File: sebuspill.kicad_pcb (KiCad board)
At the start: 2 copper layers, 67 x 26 mm, 30 parts, among them J1 Conn_01x04_Male, J2 USB_B_Micro, J3 Pinout 1, J4 Pinout 2, SW1 SW_SPDT, U1 AMS1117-3.3, U2 STM32F103C8T6, Y1 16MHz

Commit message: finished i think
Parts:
-  : renamed from U1
-  : renamed from SW1
- moved C11 6.83 mm to (150.0, 108.0), turned to -90 degrees
- moved R2 0.69 mm to (152.4, 97.5)
- renumbered D1 to LED
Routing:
- net PC13: track 0.00 -> 67.0 mm, vias 0 -> 6
- net VBUS: track 19.3 -> 80.7 mm, vias 0 -> 1
- net PB12: track 2.81 -> 54.6 mm, vias 1 -> 4
- net PC14: track 0.00 -> 26.7 mm, vias 0 -> 4
- net PB5: track 15.1 -> 34.4 mm
- net /NRST: track 18.6 -> 11.5 mm, vias 4 -> 2
- net PA15: track 8.43 -> 15.1 mm
- net +3V3: track 200.6 -> 205.6 mm
- net /BOOT0: track 10.7 -> 14.9 mm, vias 0 -> 2
- net PB3: track 10.3 -> 13.7 mm
- net GND: track 41.0 -> 43.4 mm, vias 15 -> 16
- net PA9: track 18.8 -> 16.7 mm
- net PB13: track 28.1 -> 29.2 mm
- net /SWCLK: track 28.4 -> 27.6 mm, vias 2 -> 0
- net /BOOTP_SW: track 22.8 -> 22.1 mm
- added copper zone on F.Cu, net +3V3
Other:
- board text added: "+3.3V"
- board text added: "0"
- board text added: "1"
- board text added: "2024 sebsus"
- board text added: "3.3V"
- board text added: "B3"
- board text added: "BOOTP"
- board text added: "CLK"
- board text added: "Devboard rev 0.1"
- board text added: "GND"
- board text added: "PA0"
- board text added: "PA1"
- board text added: "PA10"
- board text added: "PA15"
- board text added: "PA2"
- board text added: "PA3"
- board text added: "PA4"
- board text added: "PA5"
- board text added: "PA6"
- board text added: "PA7"
- board text added: "PA8"
- board text added: "PA9"
- board text added: "PB0"
- board text added: "PB1"
- board text added: "PB10"
- board text added: "PB11"
- board text added: "PB12"
- board text added: "PB13"
- board text added: "PB14"
- board text added: "PB15"
- board text added: "PB4"
- board text added: "PB5"
- board text added: "PB6"
- board text added: "PB7"
- board text added: "PB8"
- board text added: "PB9"
- board text added: "PC13"
- board text added: "PC14"
- board text added: "PC15"
- board text added: "STM32F103C8T6"
- board text added: "SWD"
- board text added: "Sebastian Kind"
- board text added: "USB"
- board text added: "VBUS"
- board text added: "x"

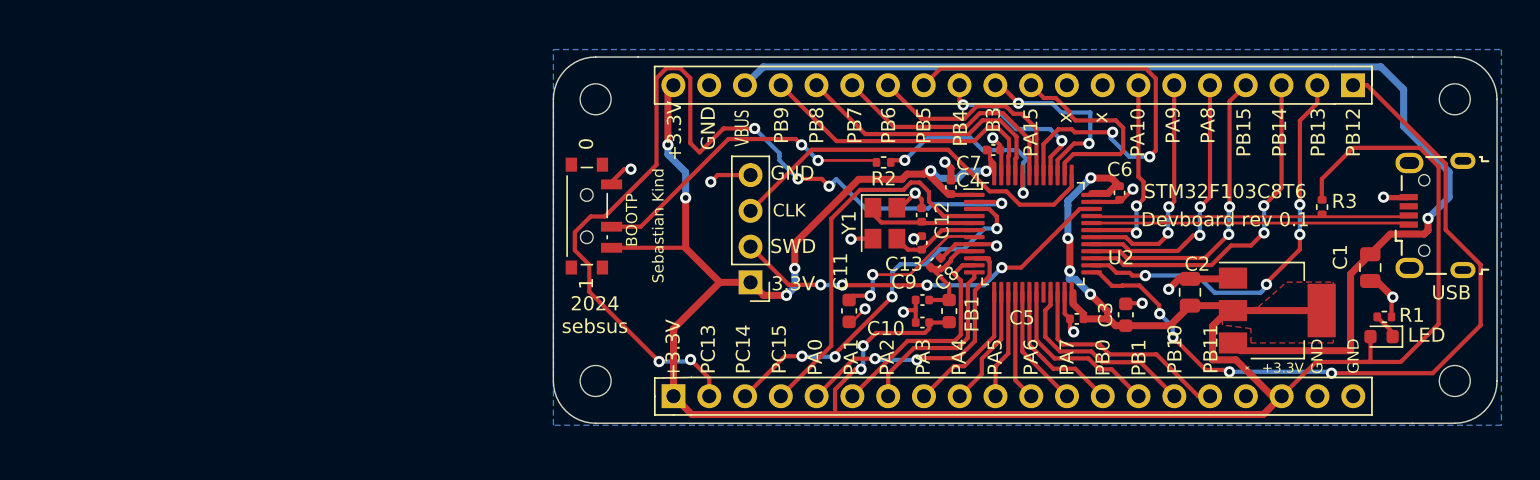
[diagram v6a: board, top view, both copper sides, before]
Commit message: changed SMD switch to Jumper bc JLCPCB hat no in stock and added User programmable LED to PC13
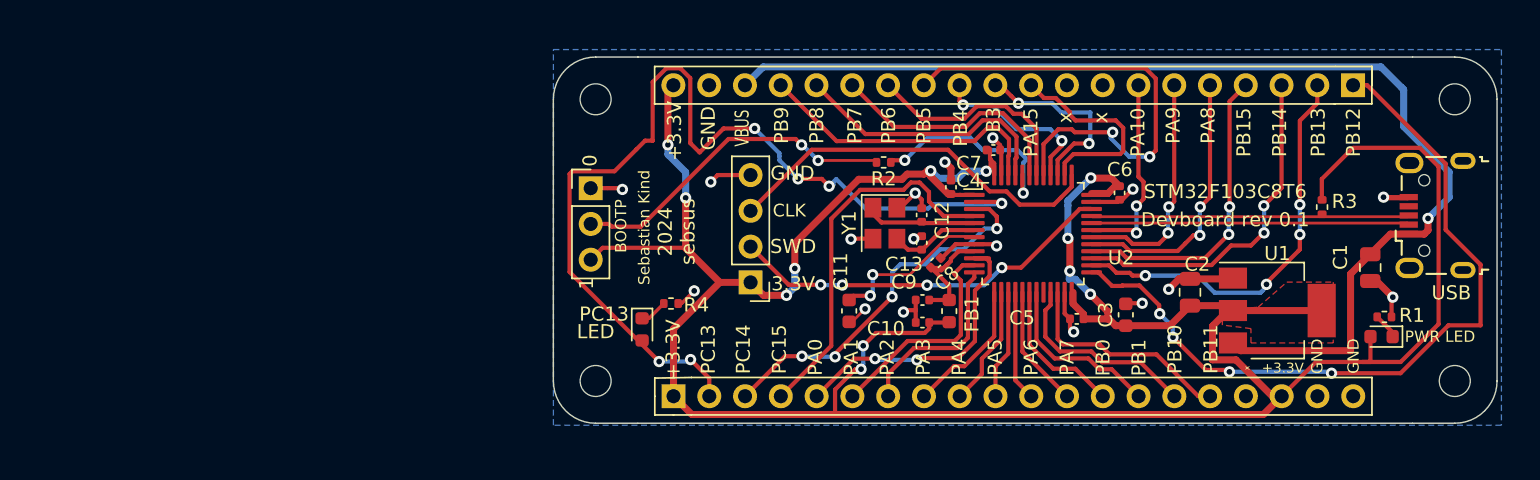
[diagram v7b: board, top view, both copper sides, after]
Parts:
- removed the   at (131.7, 101.3)
- added  : Conn_01x03_Male, Connector_PinHeader_2.54mm:PinHeader_1x03_P2.54mm_Vertical, F.Cu at (131.7, 99.3)
- added PC13: RED, LED_SMD:LED_0603_1608Metric, F.Cu at (135.3, 109.3)
- added R4: 1k5, Resistor_SMD:R_0402_1005Metric, F.Cu at (137.3, 107.5)
- PWR LED: renamed from LED
- U1: renamed from  
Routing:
- net Net-(D2-Pad1): track 0.00 -> 1.97 mm
- net GND: track 43.4 -> 45.3 mm, vias 16 -> 17
- net +3V3: track 205.6 -> 207.4 mm
- net PC13: track 67.0 -> 68.8 mm
- net /BOOTP_SW: track 22.1 -> 23.6 mm
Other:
- rule pad_to_mask_clearance: 0 -> 0.05
- board text added: "LED"

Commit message: took Jacopops Feedback <3 and rerouted some traces
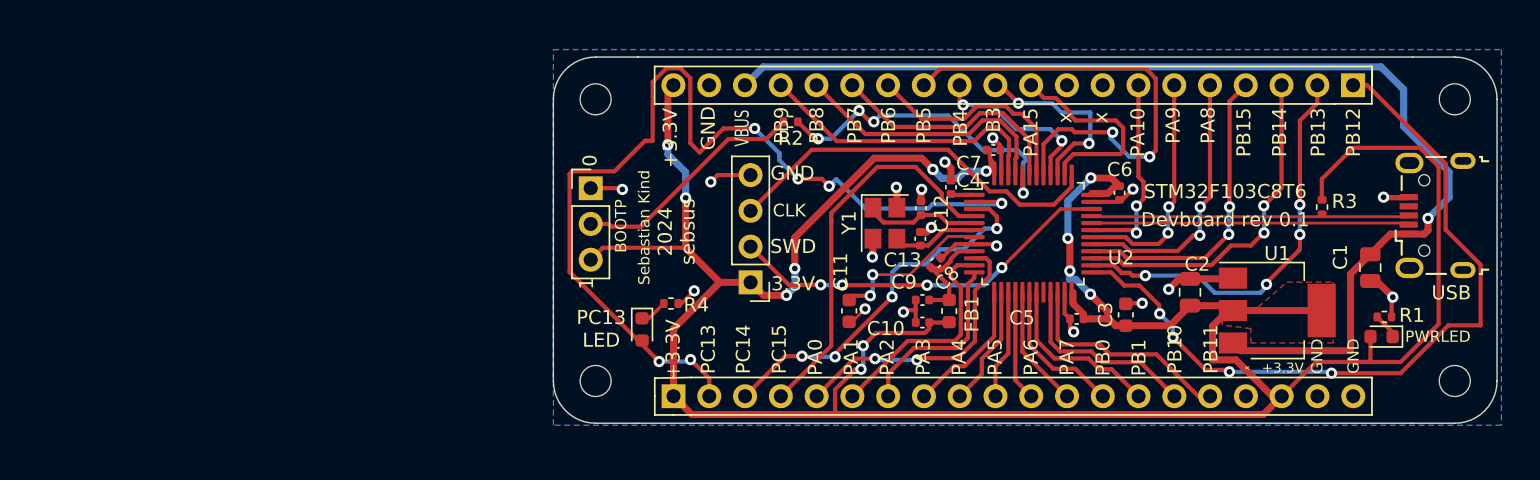
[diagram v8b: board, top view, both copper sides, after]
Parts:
- D1: renamed from PWR LED
- moved R2 7.20 mm to (145.8, 94.6)
- moved C12 0.49 mm to (155.1, 100.7)
- moved C13 0.31 mm to (155.1, 102.9)
- renumbered PC13 to D1
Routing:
- net /BOOT0: track 14.9 -> 23.2 mm, vias 2 -> 4
- net /BOOTP_SW: track 23.6 -> 16.9 mm, vias 2 -> 0
- net +3V3: track 207.4 -> 206.0 mm
- net PC15: track 26.7 -> 27.9 mm
- net PA0: track 21.5 -> 20.4 mm
- net /HSE_IN: track 7.95 -> 8.71 mm
- net GND: track 45.3 -> 44.6 mm, vias 17 -> 18
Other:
- board text added: "PC13 LED"
- board text added: "PWRLED"
- board text removed: "LED"
